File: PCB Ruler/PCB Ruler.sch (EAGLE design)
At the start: 1 part

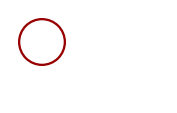
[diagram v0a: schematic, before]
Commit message: Updated website on silkscreen
Signed-off-by: Cruz Monrreal II <Cruz.Monrreal@gmail.com>
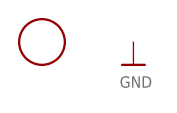
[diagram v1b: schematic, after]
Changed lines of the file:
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@@
 <layers>
 <layer number="1" name="Top" color="4" fill="1" visible="no" active="no"/>
+<layer number="2" name="Route2" color="1" fill="3" visible="no" active="no"/>
+<layer number="3" name="Route3" color="4" fill="3" visible="no" active="no"/>
+<layer number="4" name="Route4" color="1" fill="4" visible="no" active="no"/>
+<layer number="5" name="Route5" color="4" fill="4" visible="no" active="no"/>
+<layer number="6" name="Route6" color="1" fill="8" visible="no" active="no"/>
+<layer number="7" name="Route7" color="4" fill="8" visible="no" active="no"/>
+<layer number="8" name="Route8" color="1" fill="2" visible="no" active="no"/>
+<layer number="9" name="Route9" color="4" fill="2" visible="no" active="no"/>
+<layer number="10" name="Route10" color="1" fill="7" visible="no" active="no"/>
+<layer number="11" name="Route11" color="4" fill="7" visible="no" active="no"/>
+<layer number="12" name="Route12" color="1" fill="5" visible="no" active="no"/>
+<layer number="13" name="Route13" color="4" fill="5" visible="no" active="no"/>
+<layer number="14" name="Route14" color="1" fill="6" visible="no" active="no"/>
+<layer number="15" name="Route15" color="4" fill="6" visible="no" active="no"/>
 <layer number="16" name="Bottom" color="1" fill="1" visible="no" active="no"/>
 <layer number="17" name="Pads" color="2" fill="1" visible="no" active="no"/>
@@
 <layer number="109" name="fp9" color="7" fill="1" visible="yes" active="yes"/>
 <layer number="110" name="fp0" color="7" fill="1" visible="yes" active="yes"/>
+<layer number="111" name="MPL" color="7" fill="1" visible="yes" active="yes"/>
+<layer number="112" name="tSilk" color="7" fill="1" visible="yes" active="yes"/>
 <layer number="116" name="Patch_BOT" color="9" fill="4" visible="yes" active="yes"/>
 <layer number="121" name="_tsilk" color="7" fill="1" visible="yes" active="yes"/>
@@
 <layer number="123" name="tTestmark" color="7" fill="1" visible="yes" active="yes"/>
 <layer number="124" name="bTestmark" color="7" fill="1" visible="yes" active="yes"/>
+<layer number="125" name="_tNames" color="7" fill="1" visible="yes" active="yes"/>
+<layer number="126" name="_bNames" color="7" fill="1" visible="yes" active="yes"/>
+<layer number="127" name="_tValues" color="7" fill="1" visible="yes" active="yes"/>
+<layer number="128" name="_bValues" color="7" fill="1" visible="yes" active="yes"/>
 <layer number="131" name="tAdjust" color="7" fill="1" visible="yes" active="yes"/>
 <layer number="132" name="bAdjust" color="7" fill="1" visible="yes" active="yes"/>
 <layer number="144" name="Drill_legend" color="7" fill="1" visible="yes" active="yes"/>
 <layer number="151" name="HeatSink" color="7" fill="1" visible="yes" active="yes"/>
+<layer number="152" name="_bDocu" color="7" fill="1" visible="yes" active="yes"/>
 <layer number="199" name="Contour" color="7" fill="1" visible="yes" active="yes"/>
 <layer number="200" name="200bmp" color="1" fill="10" visible="yes" active="yes"/>
@@
 <layer number="215" name="215bmp" color="7" fill="1" visible="yes" active="yes"/>
 <layer number="216" name="216bmp" color="7" fill="1" visible="yes" active="yes"/>
+<layer number="248" name="Housing" color="7" fill="1" visible="yes" active="yes"/>
+<layer number="249" name="Edge" color="7" fill="1" visible="yes" active="yes"/>
 <layer number="250" name="Descript" color="3" fill="1" visible="no" active="no"/>
 <layer number="251" name="SMDround" color="12" fill="11" visible="no" active="no"/>
@@
 <part name="U$1" library="thinkmaketest" deviceset="A4_LAYOUT" device=""/>
 <part name="U$2" library="adafruit" deviceset="FIDUCIAL" device=""/>
+<part name="U$3" library="microbuilder" deviceset="GND" device=""/>
 </parts>
 <sheets>
@@
 <instance part="U$1" gate="G$1" x="0" y="0"/>
 <instance part="U$2" gate="G$1" x="109.22" y="119.38"/>
+<instance part="U$3" gate="G$1" x="119.38" y="116.84"/>
 </instances>
 <busses>
